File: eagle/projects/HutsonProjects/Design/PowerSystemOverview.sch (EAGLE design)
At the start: 27 parts, among them U1 MCP7384XX, U3 MT3608, U4 LTC3531ES6-3_3

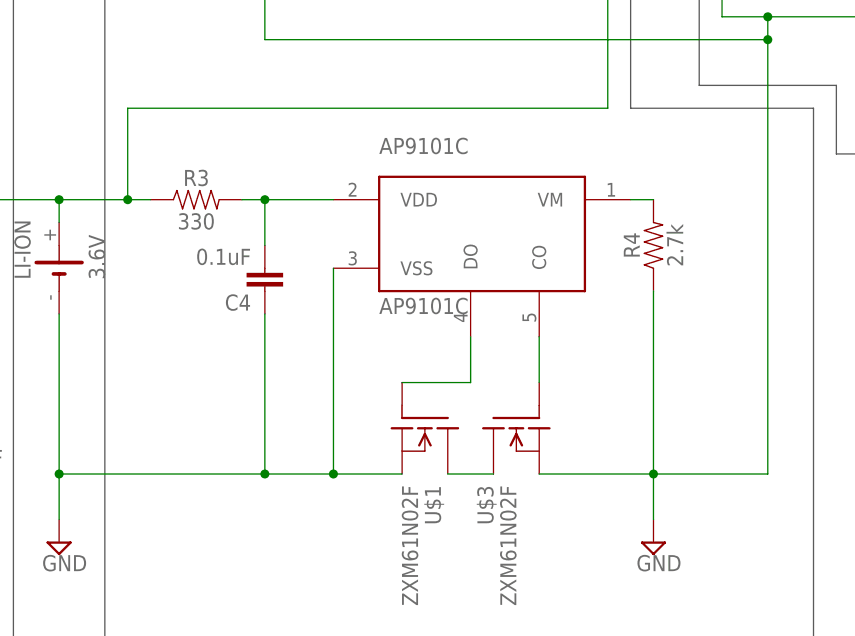
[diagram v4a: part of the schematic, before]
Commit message: 330 ohm chip resistor added
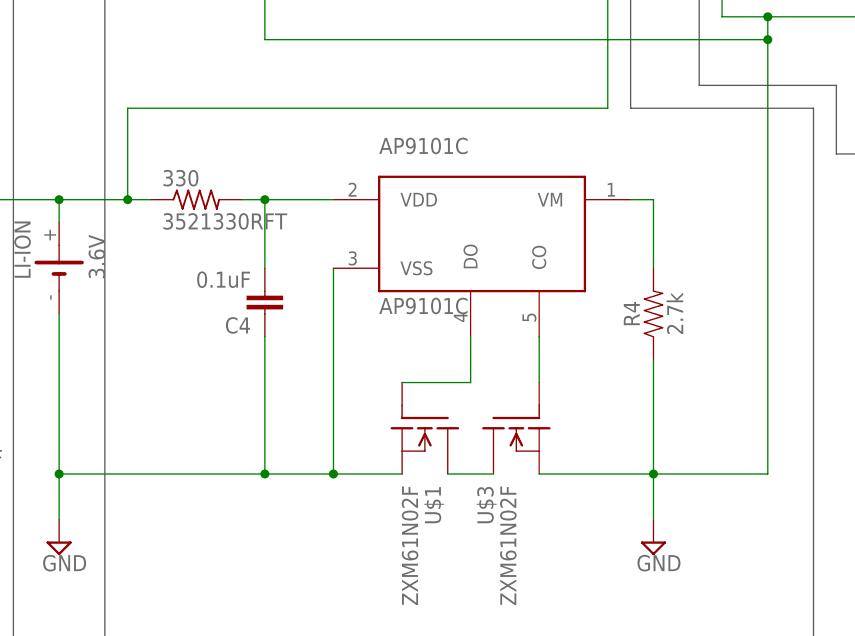
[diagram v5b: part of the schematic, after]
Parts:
- removed R3: 330, SparkFun-Resistors:330OHM-0603-1/10W-1%
- added 330: 3521330RFT, 3521330RFT:3521330RFT
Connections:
- net N$16: now also 330.1; no longer R3.1
- net N$7: now also 330.2; no longer R3.2
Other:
- moved on the sheet: C4, R4
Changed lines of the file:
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@@
 <part name="C3" library="SparkFun-Capacitors" deviceset="0.1UF" device="-0402-16V-10%" value="0.1uF"/>
 <part name="U$2" library="NDS8434" deviceset="NDS8434" device=""/>
-<part name="R3" library="SparkFun-Resistors" deviceset="330OHM" device="-0603-1/10W-1%" value="330"/>
 <part name="C4" library="SparkFun-Capacitors" deviceset="0.1UF" device="-0402-16V-10%" value="0.1uF"/>
 <part name="U$1" library="ZXM61N02F" deviceset="ZXM61N02F" device=""/>
@@
 <part name="0.1OHM" library="RL1220S-R10-F" deviceset="RL1220S-R10-F" device=""/>
 <part name="100K" library="RC0201JR-07100KL" deviceset="RC0201JR-07100KL" device=""/>
+<part name="330" library="3521330RFT" deviceset="3521330RFT" device=""/>
 </parts>
 <sheets>
@@
 </instance>
 <instance part="U$2" gate="G$1" x="55.88" y="121.92" smashed="yes" rot="R90"/>
-<instance part="R3" gate="G$1" x="104.14" y="111.76" smashed="yes">
-<attribute name="NAME" x="104.14" y="113.284" size="1.778" layer="95" font="vector" align="bottom-center"/>
-<attribute name="VALUE" x="104.14" y="110.236" size="1.778" layer="96" font="vector" align="top-center"/>
-</instance>
-<instance part="C4" gate="G$1" x="111.76" y="104.14" smashed="yes" rot="R180">
-<attribute name="NAME" x="110.236" y="101.219" size="1.778" layer="95" font="vector" rot="R180"/>
-<attribute name="VALUE" x="110.236" y="106.299" size="1.778" layer="96" font="vector" rot="R180"/>
+<instance part="C4" gate="G$1" x="111.76" y="101.6" smashed="yes" rot="R180">
+<attribute name="NAME" x="110.236" y="98.679" size="1.778" layer="95" font="vector" rot="R180"/>
+<attribute name="VALUE" x="110.236" y="103.759" size="1.778" layer="96" font="vector" rot="R180"/>
 </instance>
 <instance part="U$1" gate="G$1" x="129.54" y="86.36" smashed="yes" rot="R270">
@@
 <attribute name="NAME" x="137.157440625" y="80.0215" size="1.779790625" layer="95" rot="MR270"/>
 </instance>
-<instance part="R4" gate="G$1" x="154.94" y="106.68" smashed="yes" rot="R90">
-<attribute name="NAME" x="153.416" y="106.68" size="1.778" layer="95" font="vector" rot="R90" align="bottom-center"/>
-<attribute name="VALUE" x="156.464" y="106.68" size="1.778" layer="96" font="vector" rot="R90" align="top-center"/>
+<instance part="R4" gate="G$1" x="154.94" y="99.06" smashed="yes" rot="R90">
+<attribute name="NAME" x="153.416" y="99.06" size="1.778" layer="95" font="vector" rot="R90" align="bottom-center"/>
+<attribute name="VALUE" x="156.464" y="99.06" size="1.778" layer="96" font="vector" rot="R90" align="top-center"/>
 </instance>
 <instance part="SUPPLY5" gate="GND" x="154.94" y="73.66" smashed="yes">
@@
 <attribute name="NAME" x="8.89" y="82.7786" size="1.778" layer="95"/>
 <attribute name="VALUE" x="8.89" y="77.978" size="1.778" layer="96"/>
+</instance>
+<instance part="330" gate="G$1" x="104.14" y="111.76" smashed="yes">
+<attribute name="NAME" x="100.33" y="113.2586" size="1.778" layer="95"/>
+<attribute name="VALUE" x="100.33" y="108.458" size="1.778" layer="96"/>
 </instance>
 </instances>
@@
 <pinref part="C4" gate="G$1" pin="1"/>
 <wire x1="88.9" y1="81.28" x2="88.9" y2="76.2" width="0.1524" layer="91"/>
-<wire x1="111.76" y1="99.06" x2="111.76" y2="81.28" width="0.1524" layer="91"/>
+<wire x1="111.76" y1="96.52" x2="111.76" y2="81.28" width="0.1524" layer="91"/>
 <pinref part="U$1" gate="G$1" pin="S"/>
 <wire x1="111.76" y1="81.28" x2="119.38" y2="81.28" width="0.1524" layer="91"/>
@@
 <wire x1="154.94" y1="81.28" x2="154.94" y2="76.2" width="0.1524" layer="91"/>
 <pinref part="R4" gate="G$1" pin="1"/>
-<wire x1="154.94" y1="81.28" x2="154.94" y2="101.6" width="0.1524" layer="91"/>
+<wire x1="154.94" y1="81.28" x2="154.94" y2="93.98" width="0.1524" layer="91"/>
 <junction x="154.94" y="81.28"/>
 <wire x1="154.94" y1="81.28" x2="167.64" y2="81.28" width="0.1524" layer="91"/>
@@
 <net name="N$7" class="0">
 <segment>
-<pinref part="R3" gate="G$1" pin="2"/>
 <pinref part="U$4" gate="G$1" pin="VDD"/>
-<wire x1="109.22" y1="111.76" x2="111.76" y2="111.76" width="0.1524" layer="91"/>
 <pinref part="C4" gate="G$1" pin="2"/>
 <wire x1="111.76" y1="111.76" x2="119.38" y2="111.76" width="0.1524" layer="91"/>
-<wire x1="111.76" y1="106.68" x2="111.76" y2="111.76" width="0.1524" layer="91"/>
+<wire x1="111.76" y1="104.14" x2="111.76" y2="111.76" width="0.1524" layer="91"/>
+<pinref part="330" gate="G$1" pin="2"/>
+<wire x1="109.22" y1="111.76" x2="111.76" y2="111.76" width="0.1524" layer="91"/>
 <junction x="111.76" y="111.76"/>
 </segment>
@@
 <pinref part="U$3" gate="G$1" pin="D"/>
 <wire x1="132.08" y1="81.28" x2="137.16" y2="81.28" width="0.1524" layer="91"/>
-</segment>
-</net>
-<net name="N$9" class="0">
-<segment>
-<pinref part="R4" gate="G$1" pin="2"/>
-<pinref part="U$4" gate="G$1" pin="VM"/>
-<wire x1="154.94" y1="111.76" x2="152.4" y2="111.76" width="0.1524" layer="91"/>
 </segment>
 </net>
@@
 <pinref part="LI-ION" gate="G$1" pin="+"/>
 <wire x1="88.9" y1="109.22" x2="88.9" y2="111.76" width="0.1524" layer="91"/>
-<pinref part="R3" gate="G$1" pin="1"/>
 <wire x1="88.9" y1="111.76" x2="96.52" y2="111.76" width="0.1524" layer="91"/>
-<wire x1="96.52" y1="111.76" x2="99.06" y2="111.76" width="0.1524" layer="91"/>
 <wire x1="96.52" y1="111.76" x2="96.52" y2="121.92" width="0.1524" layer="91"/>
-<junction x="96.52" y="111.76"/>
 <wire x1="96.52" y1="121.92" x2="149.86" y2="121.92" width="0.1524" layer="91"/>
 <pinref part="C5" gate="G$1" pin="1"/>
@@
 <wire x1="83.82" y1="213.36" x2="111.76" y2="213.36" width="0.1524" layer="91"/>
 <junction x="111.76" y="213.36"/>
+<pinref part="330" gate="G$1" pin="1"/>
+<wire x1="96.52" y1="111.76" x2="99.06" y2="111.76" width="0.1524" layer="91"/>
+<junction x="96.52" y="111.76"/>
 </segment>
 </net>
@@
 </segment>
 </net>
+<net name="N$9" class="0">
+<segment>
+<pinref part="U$4" gate="G$1" pin="VM"/>
+<wire x1="152.4" y1="111.76" x2="154.94" y2="111.76" width="0.1524" layer="91"/>
+<pinref part="R4" gate="G$1" pin="2"/>
+<wire x1="154.94" y1="111.76" x2="154.94" y2="104.14" width="0.1524" layer="91"/>
+</segment>
+</net>

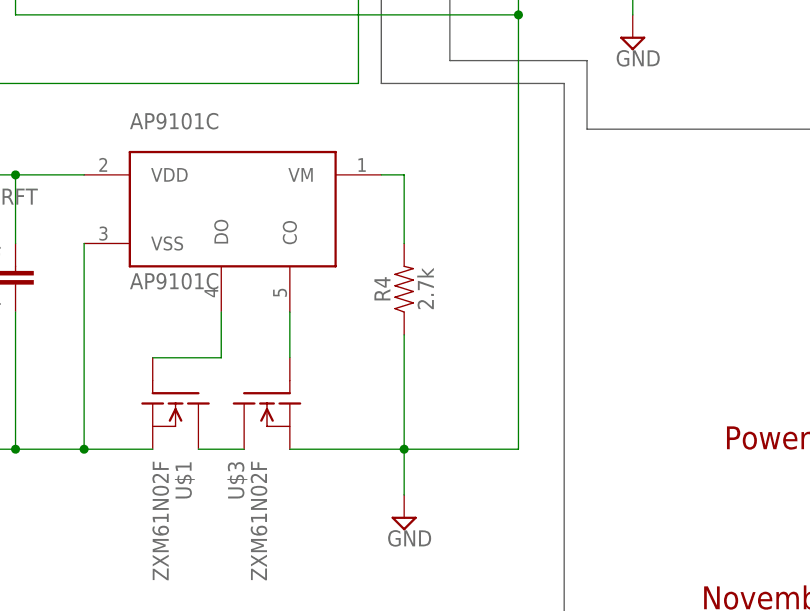
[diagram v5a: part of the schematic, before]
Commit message: 2.7k chip resistor added
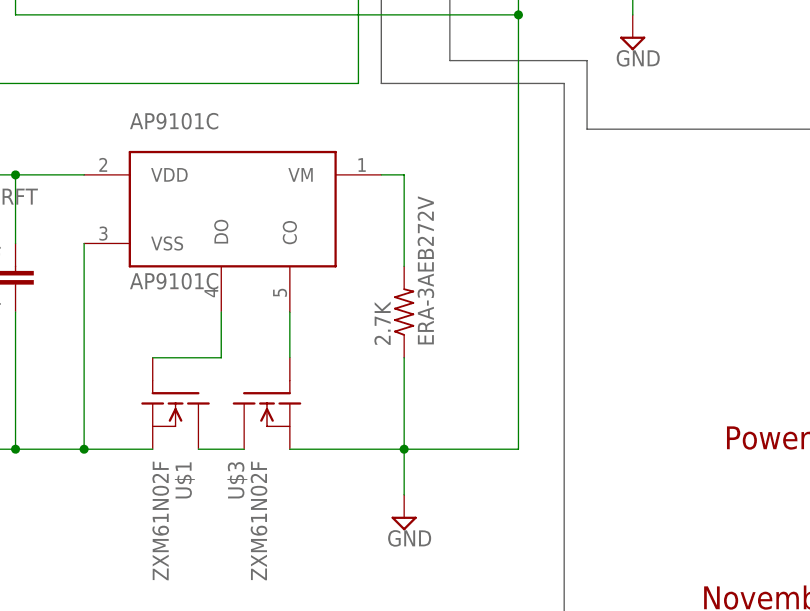
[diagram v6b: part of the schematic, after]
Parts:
- removed R4: 2.7k, SparkFun-Resistors:2.55KOHM-0603-1/10W-1%
- added 2.7K: ERA-3AEB272V, ERA-3AEB272V:ERA-3AEB272V
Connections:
- net GND: now also 2.7K.1; no longer R4.1
- net N$9: now also 2.7K.2; no longer R4.2
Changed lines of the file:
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@@
 <part name="U$1" library="ZXM61N02F" deviceset="ZXM61N02F" device=""/>
 <part name="U$3" library="ZXM61N02F" deviceset="ZXM61N02F" device=""/>
-<part name="R4" library="SparkFun-Resistors" deviceset="2.55KOHM" device="-0603-1/10W-1%" value="2.7k"/>
 <part name="SUPPLY5" library="supply2" library_urn="urn:adsk.eagle:library:372" deviceset="GND" device=""/>
 <part name="U3" library="MT3608" deviceset="MT3608" device=""/>
@@
 <part name="100K" library="RC0201JR-07100KL" deviceset="RC0201JR-07100KL" device=""/>
 <part name="330" library="3521330RFT" deviceset="3521330RFT" device=""/>
+<part name="2.7K" library="ERA-3AEB272V" deviceset="ERA-3AEB272V" device=""/>
 </parts>
 <sheets>
@@
 <attribute name="NAME" x="137.157440625" y="80.0215" size="1.779790625" layer="95" rot="MR270"/>
 </instance>
-<instance part="R4" gate="G$1" x="154.94" y="99.06" smashed="yes" rot="R90">
-<attribute name="NAME" x="153.416" y="99.06" size="1.778" layer="95" font="vector" rot="R90" align="bottom-center"/>
-<attribute name="VALUE" x="156.464" y="99.06" size="1.778" layer="96" font="vector" rot="R90" align="top-center"/>
-</instance>
 <instance part="SUPPLY5" gate="GND" x="154.94" y="73.66" smashed="yes">
 <attribute name="VALUE" x="153.035" y="70.485" size="1.778" layer="96"/>
@@
 <attribute name="NAME" x="100.33" y="113.2586" size="1.778" layer="95"/>
 <attribute name="VALUE" x="100.33" y="108.458" size="1.778" layer="96"/>
+</instance>
+<instance part="2.7K" gate="G$1" x="154.94" y="96.52" smashed="yes" rot="R90">
+<attribute name="NAME" x="153.44091875" y="92.708790625" size="1.77856875" layer="95" rot="R90"/>
+<attribute name="VALUE" x="158.242209375" y="92.709759375" size="1.778109375" layer="96" rot="R90"/>
 </instance>
 </instances>
@@
 <pinref part="SUPPLY5" gate="GND" pin="GND"/>
 <wire x1="154.94" y1="81.28" x2="154.94" y2="76.2" width="0.1524" layer="91"/>
-<pinref part="R4" gate="G$1" pin="1"/>
-<wire x1="154.94" y1="81.28" x2="154.94" y2="93.98" width="0.1524" layer="91"/>
 <junction x="154.94" y="81.28"/>
 <wire x1="154.94" y1="81.28" x2="167.64" y2="81.28" width="0.1524" layer="91"/>
@@
 <junction x="111.76" y="185.42"/>
 <junction x="167.64" y="129.54"/>
+<pinref part="2.7K" gate="G$1" pin="1"/>
+<wire x1="154.94" y1="91.44" x2="154.94" y2="81.28" width="0.1524" layer="91"/>
 </segment>
 </net>
@@
 <pinref part="U$4" gate="G$1" pin="VM"/>
 <wire x1="152.4" y1="111.76" x2="154.94" y2="111.76" width="0.1524" layer="91"/>
-<pinref part="R4" gate="G$1" pin="2"/>
-<wire x1="154.94" y1="111.76" x2="154.94" y2="104.14" width="0.1524" layer="91"/>
-</segment>
-</net>
+<pinref part="2.7K" gate="G$1" pin="2"/>
+<wire x1="154.94" y1="111.76" x2="154.94" y2="101.6" width="0.1524" layer="91"/>
+</segment>
+</net>
